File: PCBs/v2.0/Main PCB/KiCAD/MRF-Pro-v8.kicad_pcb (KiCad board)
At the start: 2 copper layers, 56.5 x 28.7 mm, 6 parts, among them J1 Feather-1, J2 Feather-2, J3 FPC 8P Connector, J4 Conn_01x08

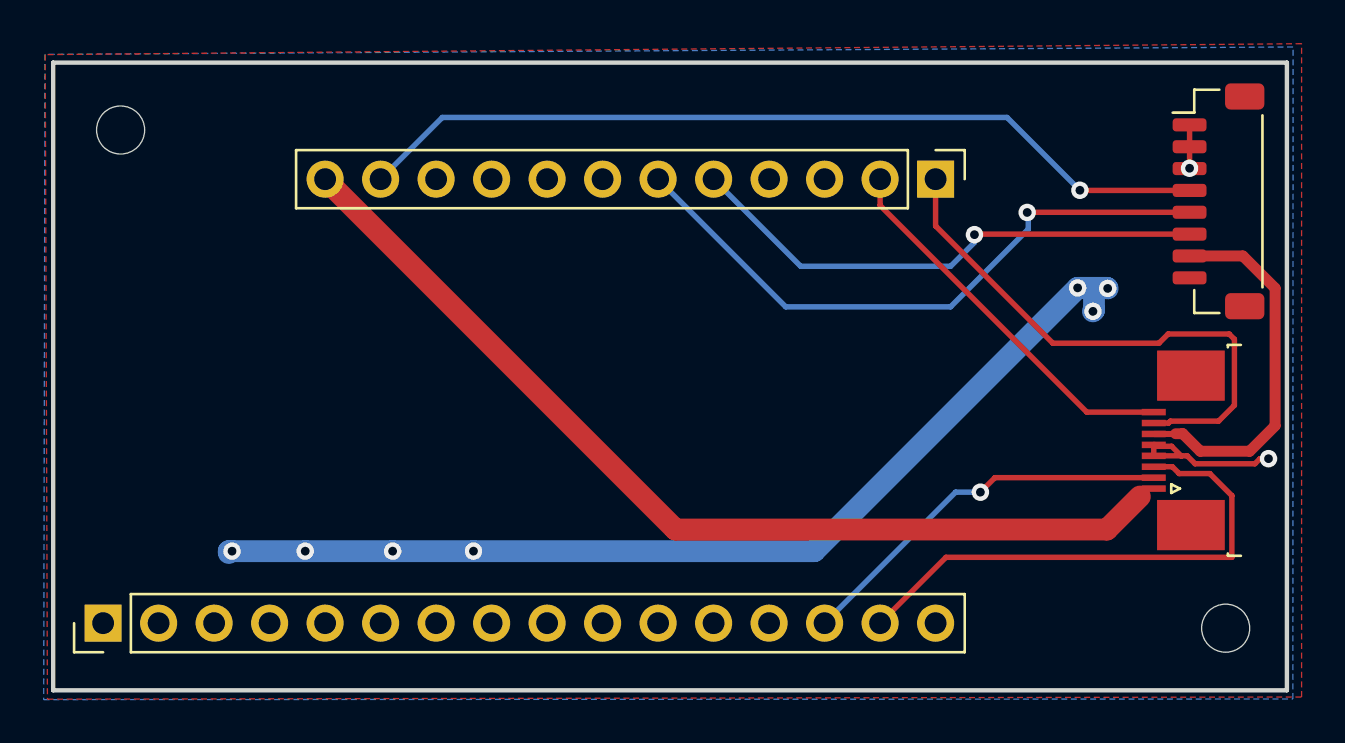
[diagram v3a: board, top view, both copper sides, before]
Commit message: MRF-Pro-v8: rework main-board power-switch nets and re-plot fab
The J4 DPDT power-switch nets were local labels named 3.3V and 3V3_SW,
which didn't read clearly and left the routing awkward. Rename them to
3.3IN (Feather 3.3 V into pole A) and 3.3OUT (switched 3.3 V out to FPC
pin 6) and make them global labels so the net role is obvious on the
sheet. Drop the now-redundant /3.3V and /GND netclass assignments,
reroute to match, and refill the pours. DRC clean: 0 violations, 0
unconnected. The breakout sheet is untouched, so its 3.3V net keeps its
name (3.3OUT on the main board = 3.3V on the breakout, joined by the FPC).

Footprint placement is unchanged, so the JLCPCB BOM and positions stay
valid. Re-plot the main-board Gerbers and drill from the reworked layout.

Sync the hardware-errata docs and the J4 diagram to the new net names,
and mark the Stage-2 LDO errata as layout-done / fab-plotted.
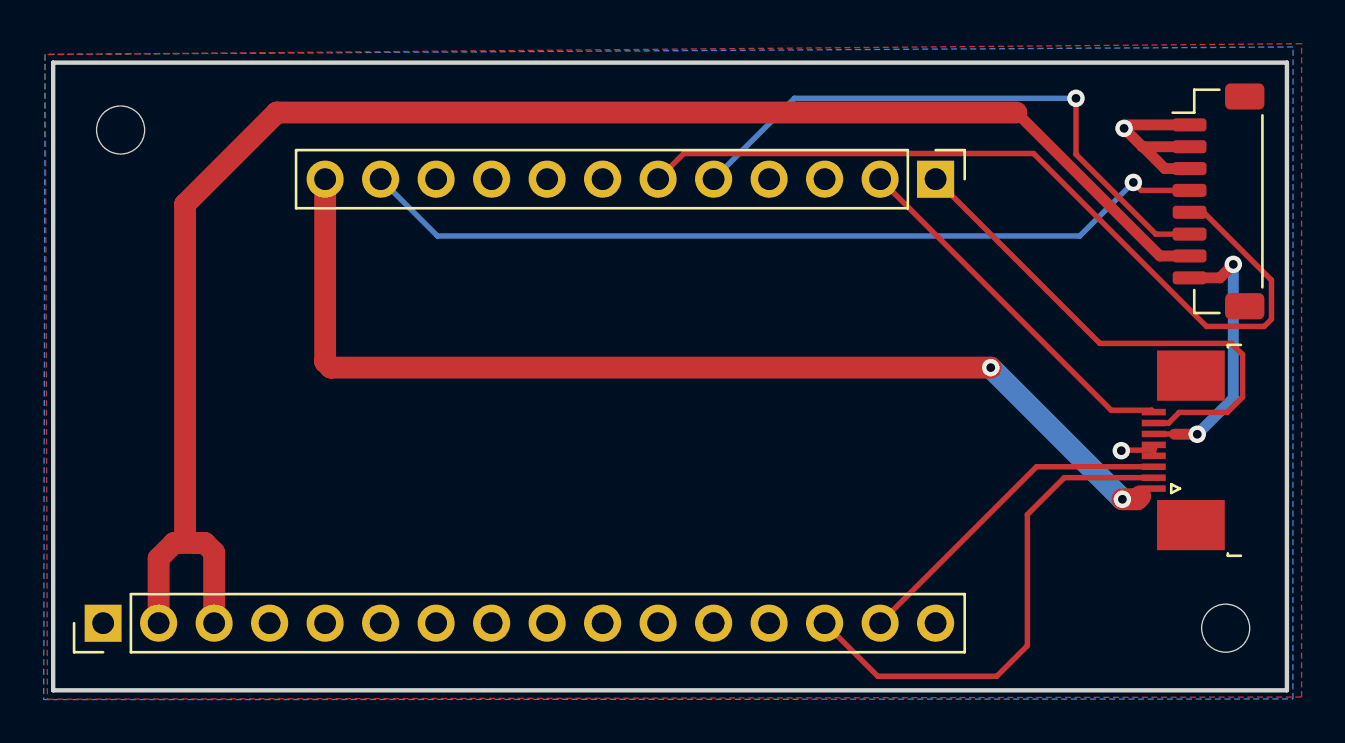
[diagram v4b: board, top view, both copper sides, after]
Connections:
- net /EN renamed EN
- net /GND renamed GND
- net /VBAT renamed VBAT
- J1 pad 2: /3.3V -> 3.3IN
- J1 pad 3: unconnected-(J1-Pin_3-Pad3) -> 3.3IN
- J3 pad 6: /3V3_SW -> 3.3OUT
- J4 pad 7: /3V3_SW -> 3.3IN
- J4 pad 8: /3.3V -> 3.3OUT
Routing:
- net 3.3IN: track 0.00 -> 75.5 mm
- net /3.3V: track 46.6 -> 0.00 mm, vias 7 -> 0
- net /3V3_SW: track 17.2 -> 0.00 mm
- net 3.3OUT: track 0.00 -> 12.7 mm, vias 0 -> 2
- net Net-(J2-Pin_6): track 29.1 -> 38.8 mm, vias 1 -> 0
- net Net-(J1-Pin_15): track 24.3 -> 15.5 mm
- net Net-(J1-Pin_14): track 17.8 -> 23.3 mm, vias 1 -> 0
- net VBAT: track 44.6 -> 48.3 mm, vias 0 -> 2
- net Net-(J2-Pin_5): track 24.3 -> 27.4 mm
- net Net-(J2-Pin_1): track 25.5 -> 23.9 mm
- net GND: track 9.47 -> 11.0 mm
- net Net-(J2-Pin_2): track 17.6 -> 16.9 mm
- added copper zone on F.Cu, net 3.3OUT
- removed copper zone on F.Cu, net /3.3V
